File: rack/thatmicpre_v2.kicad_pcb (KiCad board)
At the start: 2 copper layers, 119.1 x 74.2 mm, 81 parts, among them J1 Barrel_Jack_Switch, J2 NC3FBH1, J3 NC3MBH1, Q1 BC546C, Q2 BC546C, SW1 SW_DPDT_x2, SW2 SW_DPDT_x2, SW3 SW_Rotary12, U1 THAT1510P08-U

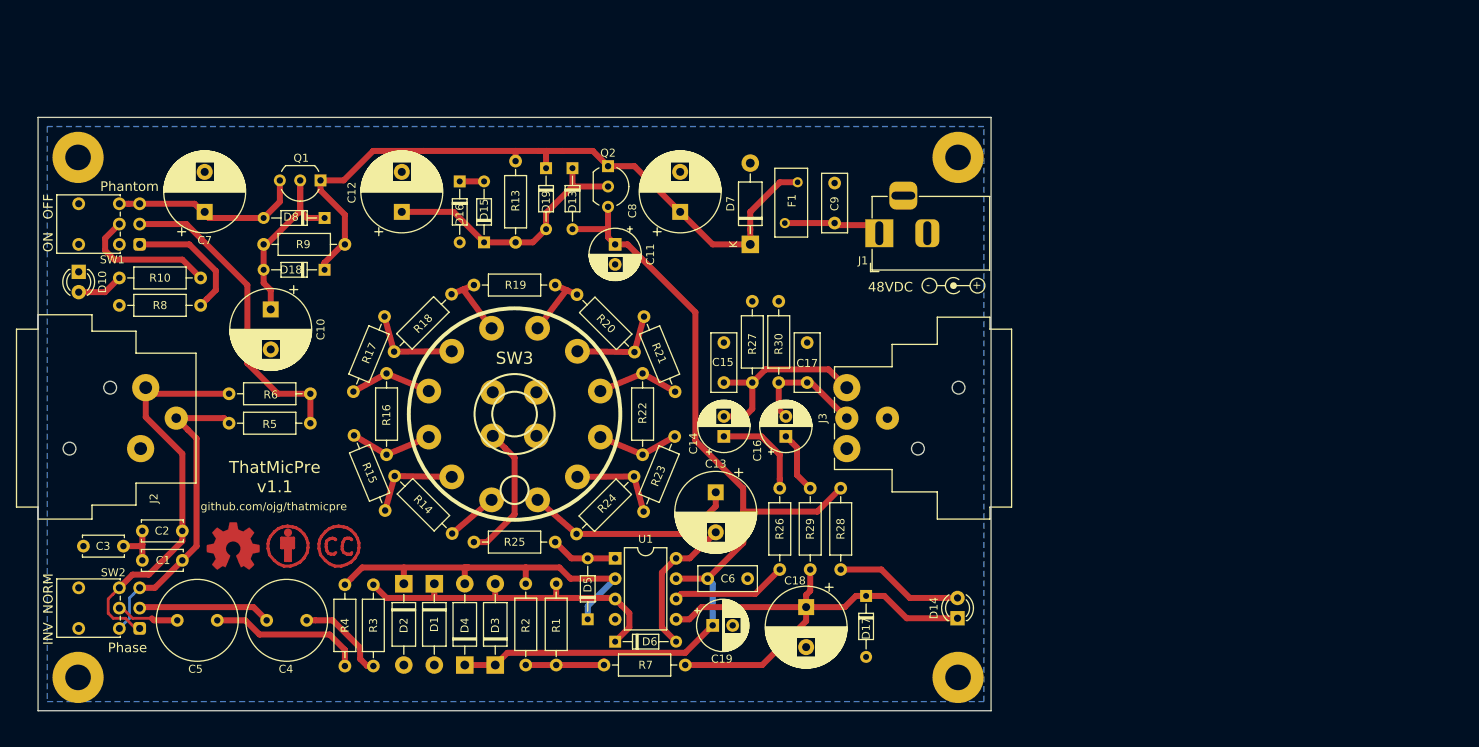
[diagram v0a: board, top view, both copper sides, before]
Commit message: First complete layout of v2
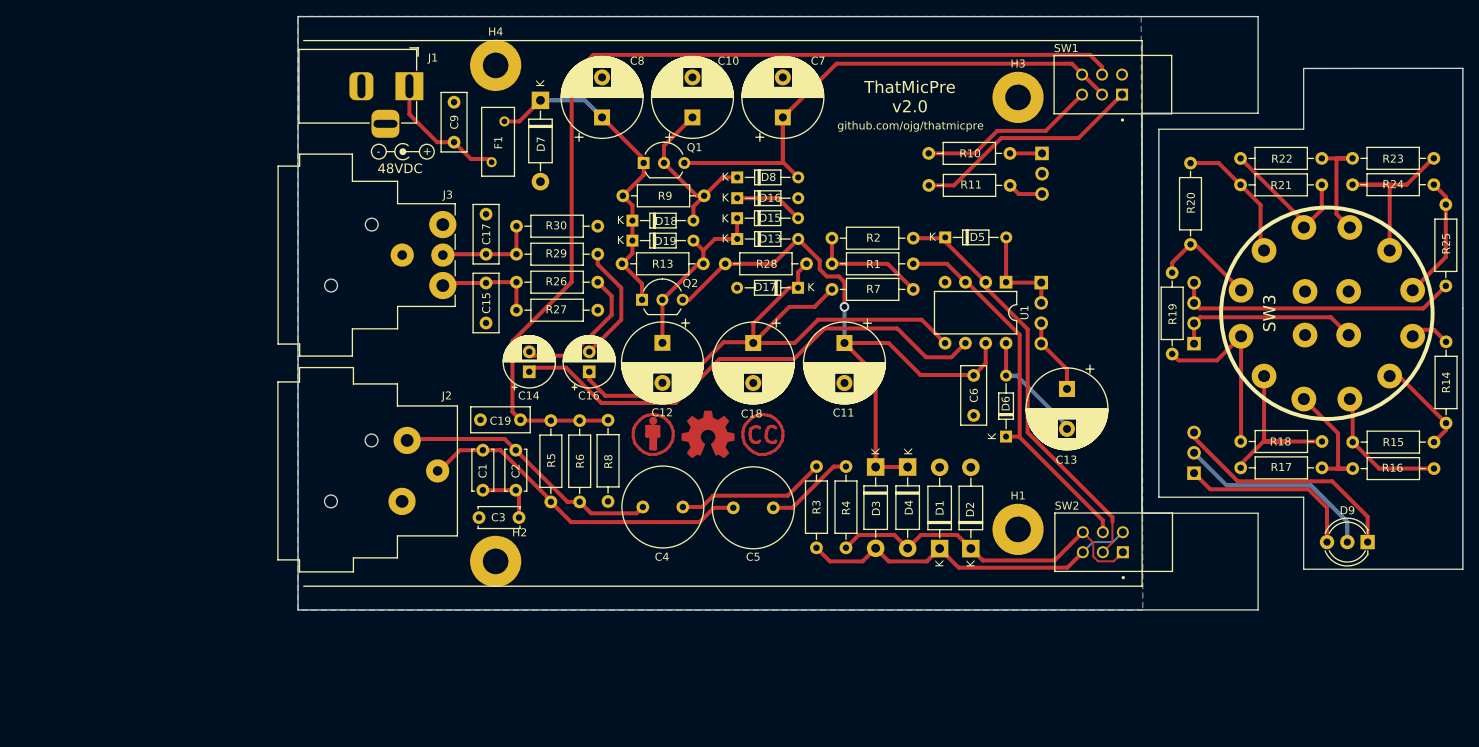
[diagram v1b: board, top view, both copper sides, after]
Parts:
- removed D10, D14: LED, LED_THT:LED_D3.0mm
- added D9: LED_Dual_AKA, LED_THT:LED_D5.0mm-3, F.Cu at (217.0, 103.9)
- added J4: Conn_01x03_Female, Connector_PinSocket_2.54mm:PinSocket_1x03_P2.54mm_Horizontal, B.Cu at (176.3, 55.3)
- added J5: Conn_01x03_Male, Connector_PinHeader_2.54mm:PinHeader_1x03_P2.54mm_Vertical, B.Cu at (195.3, 95.3)
- added J6: Conn_01x04_Female, Connector_PinSocket_2.54mm:PinSocket_1x04_P2.54mm_Horizontal, B.Cu at (176.2, 71.5)
- added J7: Conn_01x04_Male, Connector_PinHeader_2.54mm:PinHeader_1x04_P2.54mm_Vertical, B.Cu at (195.3, 79.1)
- added R11: 22k, Resistor_THT:R_Axial_DIN0207_L6.3mm_D2.5mm_P10.16mm_Horizontal, F.Cu at (162.2, 59.3)
- C11: value 47u-50V -> 220u-63V; footprint Capacitor_THT:CP_Radial_D6.3mm_P2.50mm -> Capacitor_THT:CP_Radial_D10.0mm_P5.00mm
- C19: value 47u-50V -> 100n; footprint Capacitor_THT:CP_Radial_D6.3mm_P2.50mm -> Capacitor_THT:C_Rect_L7.2mm_W3.0mm_P5.00mm_FKS2_FKP2_MKS2_MKP2
- F1: value Polyfuse -> 0ZRC0015FF1E
- J1: value Barrel_Jack_Switch -> CON-SOCJ-2155
- J2: footprint my_kicad_footprints:Jack_XLR_Neutrik_NC3FBH1_Horizontal -> Connector_Audio:Jack_XLR_Neutrik_NC3FBH1_Horizontal
- J3: footprint my_kicad_footprints:Jack_XLR_Neutrik_NC3MBH_Horizontal -> Connector_Audio:Jack_XLR_Neutrik_NC3MBH_Horizontal
- Q1, Q2: value BC546C -> BC546CTA
- SW1, SW2: value SW_DPDT_x2 -> PBH2UEESNPNAGX; footprint Button_Switch_THT:SW_Push_2P2T_Vertical_E-Switch_800UDP8P1A1M6 -> my_kicad_footprints:SW_PBH2UEESNPNAGX
- SW3: value SW_Rotary12 -> SR2612F-0112-38F5B-D8-S
- moved R14 131.6 mm to (226.8, 89.0), turned to 90 degrees
- moved H1 126.4 mm to (173.3, 102.3)
- moved R15 124.8 mm to (215.1, 91.4), turned to 0 degrees
- moved SW1 124.2 mm to (186.3, 48.0), turned to 0 degrees
- moved SW2 123.3 mm to (186.4, 105.2), turned to 0 degrees
- moved R16 121.4 mm to (215.1, 94.7), turned to 0 degrees
- moved R25 119.1 mm to (226.8, 61.7), turned to -90 degrees
- moved R24 115.7 mm to (225.3, 59.2), turned to 180 degrees
- moved R17 108.7 mm to (201.1, 94.6), turned to 0 degrees
- moved R23 108.2 mm to (225.3, 55.9), turned to 180 degrees
- moved SW3 102.3 mm to (211.9, 75.3), turned to 90 degrees
- moved R18 100.3 mm to (201.1, 91.3), turned to 0 degrees
- moved H4 95.9 mm to (108.0, 44.3)
- moved R22 92.6 mm to (211.3, 55.9), turned to 180 degrees
- moved R10 92.3 mm to (162.1, 55.3), turned to 0 degrees
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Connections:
- net Net-(C8-Pad1) renamed /VIN
- C11 pad 1: Net-(C11-Pad1) -> /V36P
- C15 pad 1: Net-(C14-Pad2) -> Net-(C15-Pad1)
- C16 pad 1: Net-(C16-Pad1) -> /V18P
- C17 pad 1: Net-(C16-Pad2) -> Net-(C17-Pad1)
- C18 pad 1: Net-(C18-Pad1) -> /V18P
- C19 pad 1: Net-(C11-Pad1) -> Net-(C19-Pad1)
- C4 pad 1: Net-(C4-Pad1) -> Net-(C2-Pad1)
- C5 pad 1: Net-(C5-Pad1) -> Net-(C1-Pad1)
- C6 pad 1: Net-(C11-Pad1) -> /V36P
- C7 pad 1: Net-(C7-Pad1) -> /V48P
- D13 pad 2: Net-(C11-Pad1) -> /V36P
- D17 pad 1: Net-(C18-Pad1) -> /V18P
- D3 pad 1: Net-(C11-Pad1) -> /V36P
- D4 pad 1: Net-(C11-Pad1) -> /V36P
- D5 pad 1: Net-(D2-Pad1) -> Net-(D5-Pad1)
- D6 pad 1: Net-(D1-Pad1) -> Net-(D6-Pad1)
- D8 pad 2: Net-(C7-Pad1) -> /V48P
- J3 pad 2: Net-(C14-Pad2) -> Net-(C15-Pad1)
- J3 pad 3: Net-(C16-Pad2) -> Net-(C17-Pad1)
- Q1 pad 3: Net-(C7-Pad1) -> /V48P
- Q2 pad 3: Net-(C11-Pad1) -> /V36P
- R1 pad 1: Net-(D1-Pad1) -> Net-(D6-Pad1)
- R2 pad 1: Net-(D2-Pad1) -> Net-(D5-Pad1)
- R24 pad 1: Net-(C13-Pad1) -> Net-(R24-Pad1)
- R25 pad 1: Net-(D5-Pad2) -> Net-(R24-Pad1)
- R25 pad 2: Net-(R25-Pad2) -> Net-(J7-Pad3)
- R26 pad 1: Net-(C14-Pad1) -> Net-(C15-Pad1)
- R26 pad 2: Net-(R26-Pad2) -> Net-(C14-Pad2)
- R27 pad 1: Net-(C14-Pad2) -> Net-(C15-Pad1)
- R28 pad 1: Net-(C11-Pad1) -> /V36P
- R28 pad 2: Net-(D14-Pad2) -> /V18P
- R29 pad 1: Net-(C16-Pad1) -> Net-(C17-Pad1)
- R29 pad 2: Net-(C18-Pad1) -> Net-(C16-Pad2)
- R30 pad 1: Net-(C16-Pad2) -> Net-(C17-Pad1)
- R5 pad 1: Net-(R5-Pad1) -> Net-(C19-Pad1)
- R6 pad 1: Net-(R5-Pad1) -> Net-(C19-Pad1)
- R7 pad 2: Net-(C18-Pad1) -> /V18P
- R8 pad 1: Net-(R8-Pad1) -> Net-(C19-Pad1)
- SW1 pad 1: Net-(R8-Pad1) -> Net-(R11-Pad1)
- SW1 pad 2: Net-(R5-Pad1) -> /V48P
- SW1 pad 3: Net-(C7-Pad1) -> Net-(R10-Pad1)
- SW1 pad 4: GND -> unconnected-(SW1-Pad4)
- SW1 pad 5: Net-(R10-Pad1) -> Net-(C19-Pad1)
- SW1 pad 6: Net-(C7-Pad1) -> /V48P
- SW2 pad 1: Net-(C2-Pad1) -> Net-(D2-Pad1)
- SW2 pad 2: Net-(C4-Pad1) -> Net-(D5-Pad1)
- SW2 pad 3: Net-(C1-Pad1) -> Net-(D1-Pad1)
- SW2 pad 4: Net-(C1-Pad1) -> Net-(D1-Pad1)
- SW2 pad 5: Net-(C5-Pad1) -> Net-(D6-Pad1)
- SW2 pad 6: Net-(C2-Pad1) -> Net-(D2-Pad1)
- SW3 pad 12: Net-(C13-Pad1) -> Net-(R24-Pad1)
- SW3 pad A: Net-(R25-Pad2) -> Net-(J7-Pad1)
- U1 pad 2: Net-(D2-Pad1) -> Net-(D5-Pad1)
- U1 pad 3: Net-(D1-Pad1) -> Net-(D6-Pad1)
- U1 pad 5: Net-(C18-Pad1) -> /V18P
- U1 pad 6: Net-(R26-Pad2) -> Net-(C14-Pad1)
- U1 pad 7: Net-(C11-Pad1) -> /V36P
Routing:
- net Net-(C19-Pad1): track 0.00 -> 126.4 mm
- net Net-(C11-Pad1): track 120.6 -> 0.00 mm
- net /V18P: track 0.00 -> 77.5 mm
- net /V36P: track 0.00 -> 77.5 mm, vias 0 -> 1
- net /V48P: track 0.00 -> 70.6 mm
- net Net-(C18-Pad1): track 61.6 -> 0.00 mm
- net Net-(D5-Pad1): track 0.00 -> 52.5 mm
- net Net-(C14-Pad1): track 12.1 -> 62.6 mm
- net Net-(D6-Pad1): track 0.00 -> 47.6 mm
- net /VIN: track 89.8 -> 42.3 mm
- net Net-(R5-Pad1): track 39.5 -> 0.00 mm
- net Net-(J7-Pad3): track 0.00 -> 35.5 mm
- net Net-(D9-Pad1): track 0.00 -> 29.6 mm
- net Net-(R11-Pad1): track 0.00 -> 28.9 mm
- net Net-(D9-Pad2): track 0.00 -> 25.3 mm
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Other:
- board size 119.1 x 74.2 mm -> 145.6 x 74.2 mm
- board text added: "ThatMicPre v2.0"
- board text removed: "INV NORM"
- board text removed: "ON OFF"
- board text removed: "Phantom"
- board text removed: "Phase"
- board text removed: "ThatMicPre v1.1"

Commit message: Redo power section layout, add PSU option
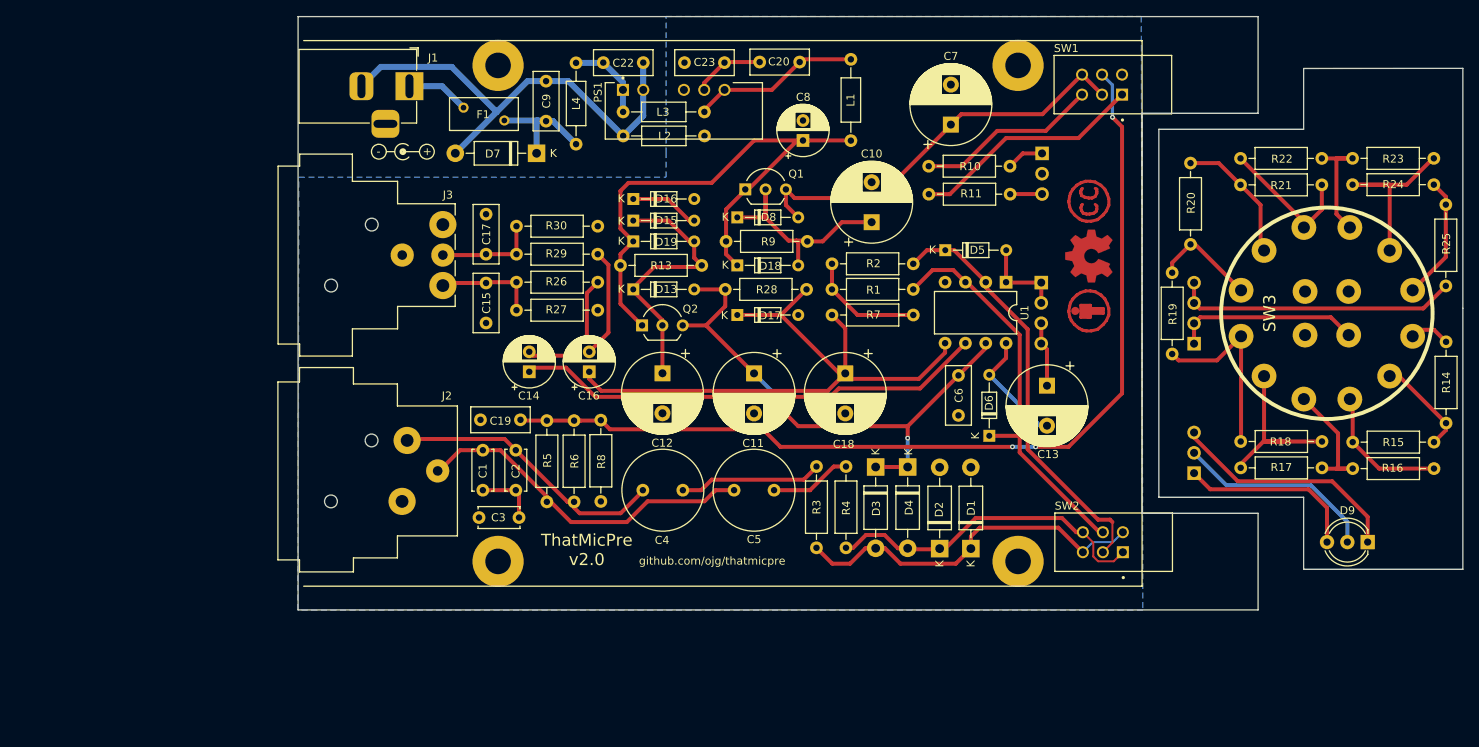
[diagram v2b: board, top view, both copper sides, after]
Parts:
- added C20: 100n, Capacitor_THT:C_Rect_L7.2mm_W3.0mm_P5.00mm_FKS2_FKP2_MKS2_MKP2, F.Cu at (146.0, 43.9)
- added C22: 4u7-25V, Capacitor_THT:C_Rect_L7.2mm_W3.0mm_P5.00mm_FKS2_FKP2_MKS2_MKP2, F.Cu at (121.5, 44.0)
- added C23: 100n, Capacitor_THT:C_Rect_L7.2mm_W3.0mm_P5.00mm_FKS2_FKP2_MKS2_MKP2, F.Cu at (136.6, 44.0)
- added L1: 4u7, Inductor_THT:L_Axial_L5.3mm_D2.2mm_P10.16mm_Horizontal_Vishay_IM-1, F.Cu at (152.4, 53.7)
- added L2: 4u7, Inductor_THT:L_Axial_L5.3mm_D2.2mm_P10.16mm_Horizontal_Vishay_IM-1, F.Cu at (134.1, 53.1)
- added L3: 4u7, Inductor_THT:L_Axial_L5.3mm_D2.2mm_P10.16mm_Horizontal_Vishay_IM-1, F.Cu at (134.1, 50.1)
- added L4: 4u7, Inductor_THT:L_Axial_L5.3mm_D2.2mm_P10.16mm_Horizontal_Vishay_IM-1, F.Cu at (118.0, 44.0)
- added PS1: PDME2-S12-D24-S, my_kicad_footprints:CONV_PDME2-S12-D24-S, F.Cu at (131.5, 50.0)
- C14, C16: value 47u-50V -> 22u-63V
- C8: value 220u-63V -> 22u-63V; footprint Capacitor_THT:CP_Radial_D10.0mm_P5.00mm -> Capacitor_THT:CP_Radial_D6.3mm_P2.50mm
- C9: value 10n -> 4u7-25V
- moved LOGO2 56.6 mm to (182.1, 75.0), turned to 90 degrees
- moved LOGO1 52.6 mm to (182.2, 68.1), turned to 90 degrees
- moved LOGO3 50.3 mm to (182.2, 61.4), turned to 90 degrees
- moved C10 25.9 mm to (155.0, 63.9)
- moved C8 25.3 mm to (146.4, 53.7)
- moved C7 21.0 mm to (164.9, 51.7)
- moved D13 14.4 mm to (125.2, 72.3)
- moved D18 14.2 mm to (138.2, 69.3)
- moved R9 14.1 mm to (136.8, 66.3)
- moved Q1 13.1 mm to (139.2, 59.8)
- moved D16 13.0 mm to (125.2, 61.0)
- moved D15 13.0 mm to (125.2, 63.7)
- moved C18 12.1 mm to (151.7, 82.8)
- moved C11 11.9 mm to (140.3, 82.8)
- moved C9 11.8 mm to (114.3, 51.3)
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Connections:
- net /V36P renamed /V35P
- C9 pad 1: Net-(C9-Pad1) -> Net-(D7-Pad1)
- C9 pad 2: GND -> Net-(J1-Pad2)
- D7 pad 1: /VIN -> Net-(D7-Pad1)
- D7 pad 2: GND -> Net-(J1-Pad2)
- F1 pad 1: Net-(C9-Pad1) -> Net-(F1-Pad1)
- F1 pad 2: /VIN -> Net-(D7-Pad1)
- H4 pad 1: GND -> unconnected-(H4-Pad1)
- J1 pad 1: Net-(C9-Pad1) -> Net-(F1-Pad1)
- J1 pad 2: GND -> Net-(J1-Pad2)
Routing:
- net Net-(J1-Pad2): track 0.00 -> 58.0 mm
- net /VIN: track 42.3 -> 71.5 mm
- net Net-(L1-Pad2): track 0.00 -> 21.2 mm
- net /V48P: track 70.6 -> 51.6 mm
- net Net-(C9-Pad1): track 16.3 -> 0.00 mm
- net Net-(D7-Pad1): track 0.00 -> 14.3 mm
- net Net-(C12-Pad1): track 23.2 -> 34.2 mm
- net Net-(C22-Pad1): track 0.00 -> 10.6 mm
- net /V35P: track 77.5 -> 67.1 mm, vias 1 -> 2
- net Net-(C23-Pad1): track 0.00 -> 8.88 mm
- net Net-(F1-Pad1): track 0.00 -> 7.87 mm
- net Net-(C10-Pad1): track 22.6 -> 29.2 mm
- net Net-(C19-Pad1): track 126.4 -> 121.1 mm, vias 0 -> 3
- net Net-(C14-Pad1): track 62.6 -> 59.0 mm
- net Net-(D6-Pad1): track 47.6 -> 50.7 mm
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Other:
- board text removed: "48VDC"

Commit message: Remove PSU option
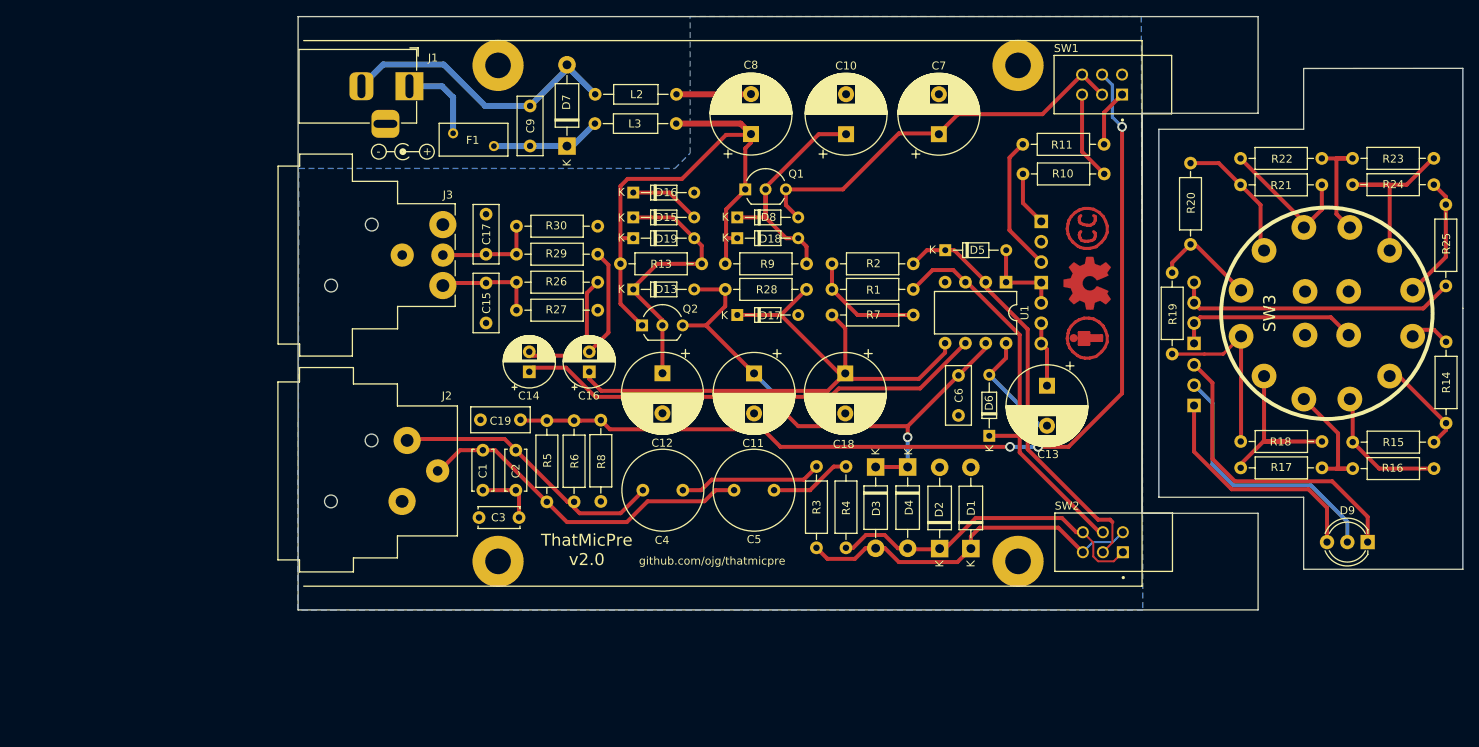
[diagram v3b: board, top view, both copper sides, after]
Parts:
- removed C20, C23: 100n, Capacitor_THT:C_Rect_L7.2mm_W3.0mm_P5.00mm_FKS2_FKP2_MKS2_MKP2
- removed C22: 4u7-25V, Capacitor_THT:C_Rect_L7.2mm_W3.0mm_P5.00mm_FKS2_FKP2_MKS2_MKP2
- removed L1, L4: 4u7, Inductor_THT:L_Axial_L5.3mm_D2.2mm_P10.16mm_Horizontal_Vishay_IM-1
- removed PS1: PDME2-S12-D24-S, my_kicad_footprints:CONV_PDME2-S12-D24-S
- C8: value 22u-63V -> 220u-63V; footprint Capacitor_THT:CP_Radial_D6.3mm_P2.50mm -> Capacitor_THT:CP_Radial_D10.0mm_P5.00mm
- C9: value 4u7-25V -> 100n
- moved R11 22.8 mm to (184.1, 54.2), turned to 180 degrees
- moved R10 22.0 mm to (184.1, 57.9), turned to 180 degrees
- moved C10 11.5 mm to (151.8, 52.9)
- moved J4 8.50 mm to (176.2, 63.8)
- moved J5 8.46 mm to (195.3, 86.8)
- moved C8 6.55 mm to (139.9, 52.9)
- moved L2 6.27 mm to (130.6, 47.9)
- moved D7 3.91 mm to (116.9, 54.4), turned to 90 degrees
- moved L3 3.81 mm to (130.6, 51.6)
- moved C9 3.69 mm to (112.3, 54.4)
- moved F1 3.45 mm to (102.7, 52.8)
- moved LOGO1 3.41 mm to (182.0, 71.5)
- moved LOGO3 3.41 mm to (182.0, 64.8)
- moved LOGO2 3.41 mm to (181.9, 78.4)
- moved D18 3.40 mm to (138.2, 65.9)
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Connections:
- C9 pad 1: Net-(D7-Pad1) -> Net-(C9-Pad1)
- D7 pad 1: Net-(D7-Pad1) -> Net-(C9-Pad1)
- F1 pad 2: Net-(D7-Pad1) -> Net-(C9-Pad1)
- L3 pad 1: Net-(L1-Pad2) -> /VIN
- L3 pad 2: Net-(C22-Pad1) -> Net-(C9-Pad1)
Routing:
- net Net-(R11-Pad1): track 29.3 -> 7.15 mm
- net Net-(C9-Pad2): track 58.0 -> 36.6 mm
- net Net-(L1-Pad2): track 21.2 -> 0.00 mm
- net Net-(D7-Pad1): track 14.3 -> 0.00 mm
- net Net-(C9-Pad1): track 0.00 -> 13.8 mm
- net Net-(J4-Pad3): track 4.00 -> 17.0 mm
- net Net-(R10-Pad1): track 22.9 -> 11.1 mm
- net Net-(C22-Pad1): track 10.6 -> 0.00 mm
- net GND: track 0.00 -> 9.37 mm
- net Net-(C23-Pad1): track 8.88 -> 0.00 mm
- net Net-(D9-Pad1): track 29.6 -> 38.3 mm
- net Net-(D9-Pad2): track 25.3 -> 33.3 mm
- net Net-(D9-Pad3): track 22.7 -> 29.6 mm
- net /VIN: track 71.5 -> 68.0 mm
- net Net-(C10-Pad1): track 29.2 -> 32.4 mm
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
